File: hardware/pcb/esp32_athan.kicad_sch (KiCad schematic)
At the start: 35 parts, among them J1 USB_C_Receptacle_PowerOnly_6P, J2 02x03_gain, J3 Speaker, J4 OLED, J5 Relay, J6 PROG, SW1 Next, SW2 Select, U1 ESP32-S3-WROOM-1-N16R8, U3 AMS1117-3.3, U4 MAX98357A

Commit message: layout finished and ready for test production
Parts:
- removed J2: 02x03_gain, Package_SO:SOIC-8_3.9x4.9mm_P1.27mm, symbol Connector_Generic:Conn_02x03_Odd_Even
- removed R6: 100k, Package_DIP:DIP-8_W7.62mm, symbol Device:R
- added JP2: SolderJumper_2_Bridged, Jumper:SolderJumper-2_P1.3mm_Bridged_RoundedPad1.0x1.5mm, symbol Jumper:SolderJumper_2_Bridged
- added JP3: SolderJumper_3_Open, Jumper:SolderJumper-3_P1.3mm_Open_RoundedPad1.0x1.5mm, symbol Jumper:SolderJumper_3_Open
- C1: footprint (none) -> Capacitor_THT:CP_Radial_D10.0mm_P5.00mm_P7.50mm
- C2, C6: value 10µF -> 22µF; footprint Package_SO:SOIC-8_3.9x4.9mm_P1.27mm -> Capacitor_SMD:C_1206_3216Metric
- C3, C4, C5, C7: footprint Package_SO:SOIC-8_3.9x4.9mm_P1.27mm -> Capacitor_SMD:C_1206_3216Metric
- D1: footprint (none) -> LED_SMD:LED_1206_3216Metric_Pad1.42x1.75mm_HandSolder
- H1, H2, H3, H4: footprint (none) -> MountingHole:MountingHole_3.2mm_M3
- J3, J5: footprint (none) -> TerminalBlock:TerminalBlock_MaiXu_MX126-5.0-02P_1x02_P5.00mm
- J4: footprint (none) -> Connector_PinHeader_2.54mm:PinHeader_1x04_P2.54mm_Vertical
- J6: footprint (none) -> Connector_PinHeader_2.54mm:PinHeader_1x06_P2.54mm_Vertical
- JP1: footprint (none) -> Jumper:SolderJumper-2_P1.3mm_Bridged_RoundedPad1.0x1.5mm
- R1, R2: value 5.1k -> 4.7k; footprint Package_DIP:DIP-8_W7.62mm -> Resistor_SMD:R_1206_3216Metric
- R10, R5, R8, R9: footprint Package_DIP:DIP-8_W7.62mm -> Resistor_SMD:R_1206_3216Metric
- R11: value 100 -> (100); footprint Package_DIP:DIP-8_W7.62mm -> Resistor_SMD:R_1206_3216Metric
- R3, R4: value 10k -> 4.7k; footprint Package_DIP:DIP-8_W7.62mm -> Resistor_SMD:R_1206_3216Metric
- R7: value 100k -> (100k); footprint Package_DIP:DIP-8_W7.62mm -> Resistor_SMD:R_1206_3216Metric
- SW1, SW2: footprint (none) -> Button_Switch_THT:SW_SPST_Omron_B3F-40xx
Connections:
- net +5V: now also JP3.3 (B)
- net GAIN: now also JP3.2 (C)
- net GND: now also J5.1 (Pin_1), JP2.1 (A); no longer J5.2 (Pin_2)
- net RLY+: now also J5.2 (Pin_2); no longer J5.1 (Pin_1)
- net at R7.1: now also JP2.2 (B), JP3.1 (A)
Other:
- moved on the sheet: J3, J5, R7

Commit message: update schematic and layout with new resistance and new 5-way button instead of select,next
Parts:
- removed SW1: Next, Button_Switch_THT:SW_SPST_Omron_B3F-40xx, symbol Switch:SW_Push
- removed SW2: Select, Button_Switch_THT:SW_SPST_Omron_B3F-40xx, symbol Switch:SW_Push
- added SW1: SKRHABE010, SKRHABE010:SW-SMD_SKRHABE010, symbol SKRHABE010:SKRHABE010
- R5: value 560k -> 4.7k
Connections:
- net BTN_SELECT: now also SW1.2 (CEN)
- net GND: now also SW1.5 (COM)
- net BTN_UP: now reaches U1.22 (IO14)
- net BTN_UP: now also SW1.1 (A)
- net BTN_LEFT: now reaches U1.23 (IO21)
- net BTN_LEFT: now also SW1.3 (C)
- net BTN_RIGHT: now reaches U1.24 (IO47)
- net BTN_RIGHT: now also SW1.4 (D)
- net BTN_NEXT renamed BTN_DOWN
- net BTN_DOWN: now also SW1.6 (B)
- no-connect marks 23 -> 22

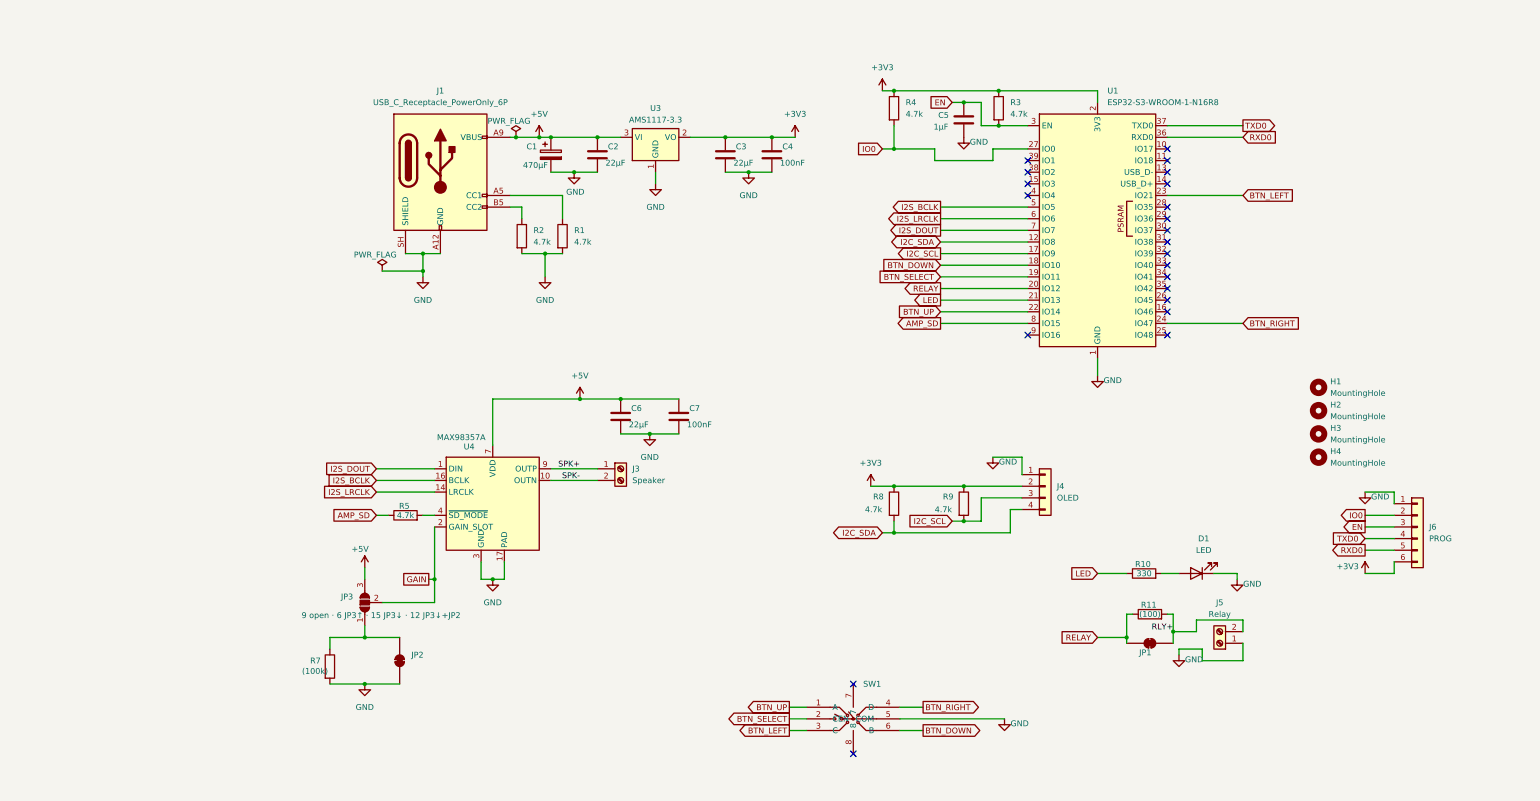
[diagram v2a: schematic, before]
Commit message: Add colour TFT build option, screen settings and the drawn PCB
Display
- The display is chosen at build time: display_type oled|tft, or --display in
  build_firmware.sh and flash_firmware.sh. Each display's code lives in
  firmware/displays/{oled,tft}.yaml. A TFT build has its own release files and
  manifest (manifest-tft.json), so a clock only updates to its own build.
- 240x240 ST7789 TFT (mipi_spi):
  - a ring clock with seconds, flashing 500/500 ms in the last minute
    before an athan;
  - a prayer strip, and mute icons for prayers whose athan is off;
  - a two-pane colour menu with Material Symbols icons;
  - Screen Colour (5 palettes) and a colour Wi-Fi setup screen.
- The OLED drawing is unchanged, behind ATHAN_DISPLAY_TFT. Both displays read
  the menu from one Frame (menu_frame.h).

Screen settings (both displays, menu and web page)
- Brightness 0-100 % (0 % = dark until a key).
- Screen at Night: Off / Dim / Dark, with Night From and Night Until.
- While the screen is dark, a key lights it, dim, for 2 min with a countdown.
- The tick and night windows can end at a prayer (From Maghrib/Isha, Until
  Fajr/Dhuhr), worked out from each day's times (day_window.h, host-tested).
  The window rows are now choices confirmed with Select, with a caption
  previewing the result.

Audio
- Fix a flash preview that kept playing after leaving its menu row: a preview
  still waiting to start is now dropped (cancel_pending_slot_preview_).
- The menu tones are mono 16-bit WAV (no decoding, no MP3 padding). Stored
  sounds stay MP3.

Hardware
- PCB drawn in KiCad: OLED header J4, TFT header J7, 5-way switch footprints
  and 3D models, renders and a STEP export.

README
- 1.1: the clock joins 2.4 GHz Wi-Fi only.
- 1.2 Screen: the OLED's timetable screen and its marks, the colour screen
  (ring, strip, last-minute flash, athan colour, Screen Colour), and the
  dark screen waking on a key.
- 1.3 Menu: two panes, short names, the new rows (Tick From/Until,
  Brightness, Screen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
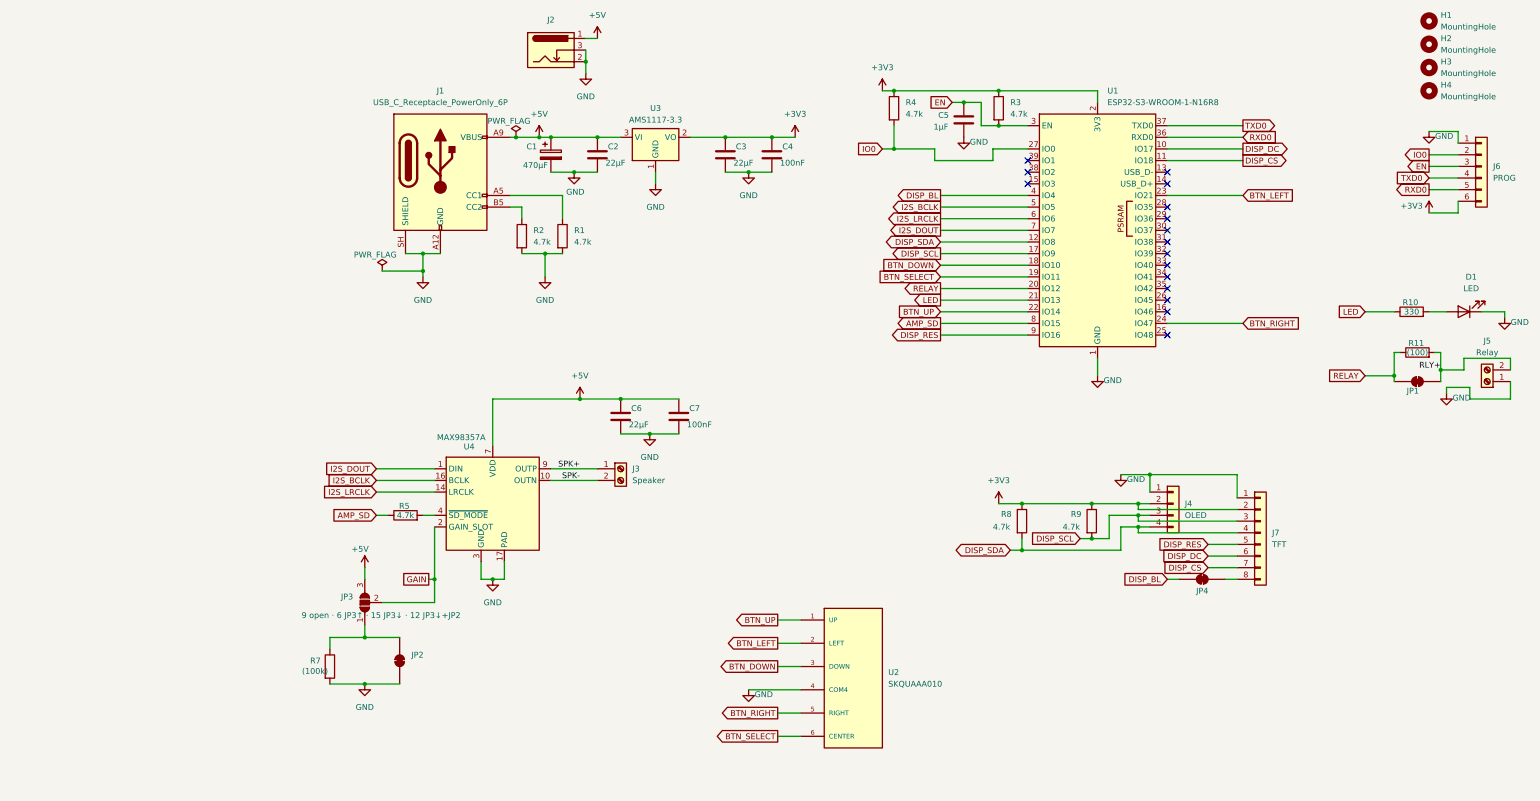
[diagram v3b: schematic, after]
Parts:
- removed SW1: SKRHABE010, SKRHABE010:SW-SMD_SKRHABE010, symbol SKRHABE010:SKRHABE010
- added J2: Barrel_Jack, Connector_BarrelJack:BarrelJack_CUI_PJ-102AH_Horizontal, symbol Connector:Barrel_Jack_Switch
- added J7: TFT, Connector_PinHeader_2.54mm:PinHeader_1x08_P2.54mm_Vertical, symbol Connector_Generic:Conn_01x08
- added JP4: SolderJumper_2_Bridged, Jumper:SolderJumper-2_P1.3mm_Bridged_RoundedPad1.0x1.5mm, symbol Jumper:SolderJumper_2_Bridged
- added U2: SKQUAAA010, SKQUAAA010:SKQUAAA010, symbol SKQUAAA010:SKQUAAA010
- C1: footprint Capacitor_THT:CP_Radial_D10.0mm_P5.00mm_P7.50mm -> Capacitor_SMD:CP_Elec_8x10.5
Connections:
- net +3V3: now also J7.2 (Pin_2)
- net +5V: now also J2.1
- net BTN_DOWN: now also U2.3 (DOWN)
- net BTN_LEFT: now also U2.2 (LEFT)
- net BTN_RIGHT: now also U2.5 (RIGHT)
- net BTN_SELECT: now also U2.6 (CENTER)
- net BTN_UP: now also U2.1 (UP)
- net GND: now also J2.2, J2.3, J7.1 (Pin_1), U2.4 (COM4)
- net DISP_DC: now reaches U1.10 (IO17)
- net DISP_DC: now also J7.6 (Pin_6)
- net DISP_CS: now reaches U1.11 (IO18)
- net DISP_CS: now also J7.7 (Pin_7)
- net DISP_BL: now reaches U1.4 (IO4)
- net DISP_BL: now also JP4.1 (A)
- net DISP_RES: now reaches U1.9 (IO16)
- net DISP_RES: now also J7.5 (Pin_5)
- net I2C_SCL renamed DISP_SCL
- net DISP_SCL: now also J7.3 (Pin_3)
- net I2C_SDA renamed DISP_SDA
- net DISP_SDA: now also J7.4 (Pin_4)
- new net: J7.8 (Pin_8), JP4.2 (B)
- no-connect marks 22 -> 16
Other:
- moved on the sheet: D1, H1, H2, H3, H4, J4, J5, J6, JP1, R10, R11, R8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

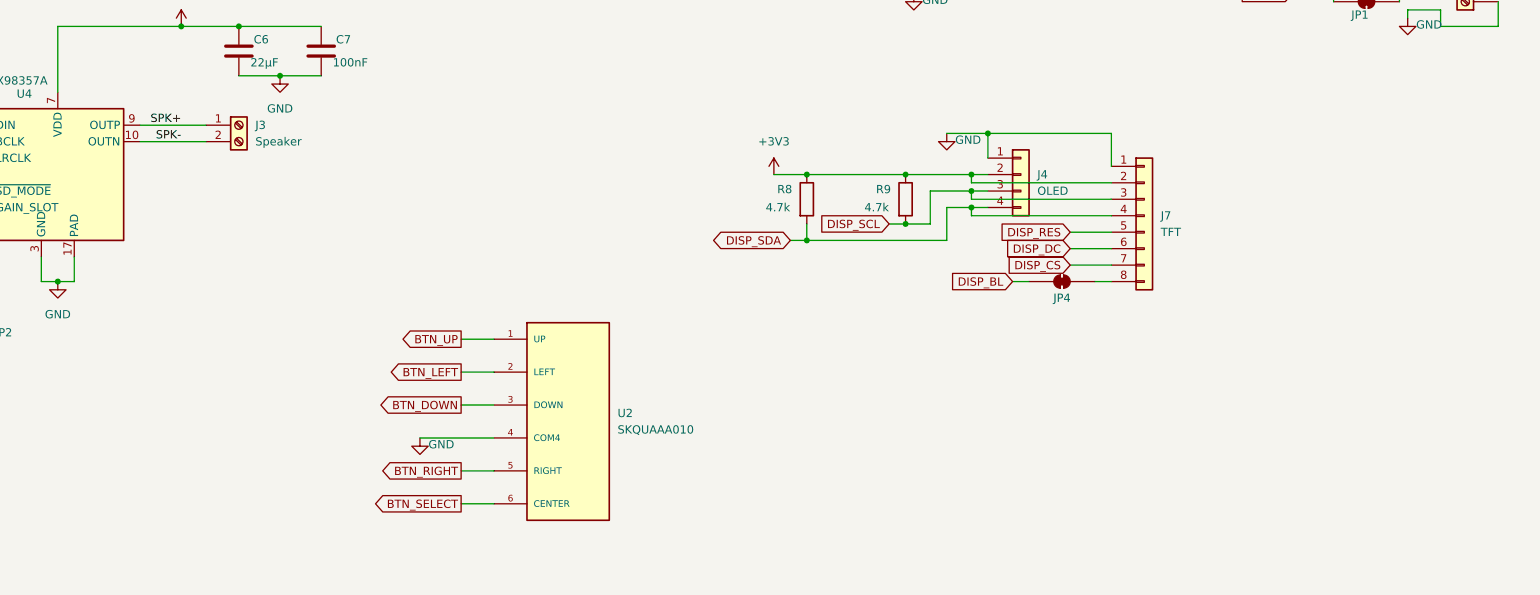
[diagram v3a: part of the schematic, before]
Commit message: Lists of any length, full code review fixes, 44.1 kHz sounds, PCB v5
Sound lists
- The suggested lists (athan, Fajr, tawashih, tick) can have any number of
  entries, numbered in file order ("2. Abdul Basit") in the menu, on /audio
  and on the web page; long names wrap or shorten to fit both displays.
- /audio: one form per sound, with its whole list in a dropdown (the one in
  use marked with a check mark) and Preview / Download buttons; the status
  bar says "downloaded and in use" and offers Reload page when the lists change.
- Radio stays at 10 stations; README shows how to add one from mp3quran.net,
  with screenshots.

Screen and windows
- Tick window: from Fajr or Dhuhr until Maghrib or Isha; night window the
  other way round. An end a window no longer offers becomes an hour at boot.
- Screen at Night: Normal (same as by day) / Dim / Turned off. Normal ignores
  the night window; Dim is never brighter than by day.
- New Night Window line on the web page; both window lines update within
  100 ms of a change.

TFT clock face
- Most seconds redraw only the seconds (about 2.5 ms instead of a 50 ms whole
  face). The whole face is redrawn every 30 s, at each minute, on any change,
  and every second in the last minute.
- The ring is drawn in one pass (tft::ring), pixel-identical to a plain scan
  over 5,820 host-tested cases.
- Frames follow the clock's own second. The last-minute flash is exactly
  500 ms lit / 500 ms dark (measured on the prototype).

Fixes from a full code review (tested on the prototype)
- An upload that broke off left every download "Busy" until a restart.
  It is now freed after 20 s.
- Saving a sound froze the clock for seconds and restarted the I2S speaker
  under the radio. Erases now go block by block with pauses, the radio
  pauses for the write, and the read-back check runs on the worker.
- A stored sound whose end the player lost could not be stopped by the
  5 s bound. Its resampler is now stopped. Joined or damaged MP3 uploads
  a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
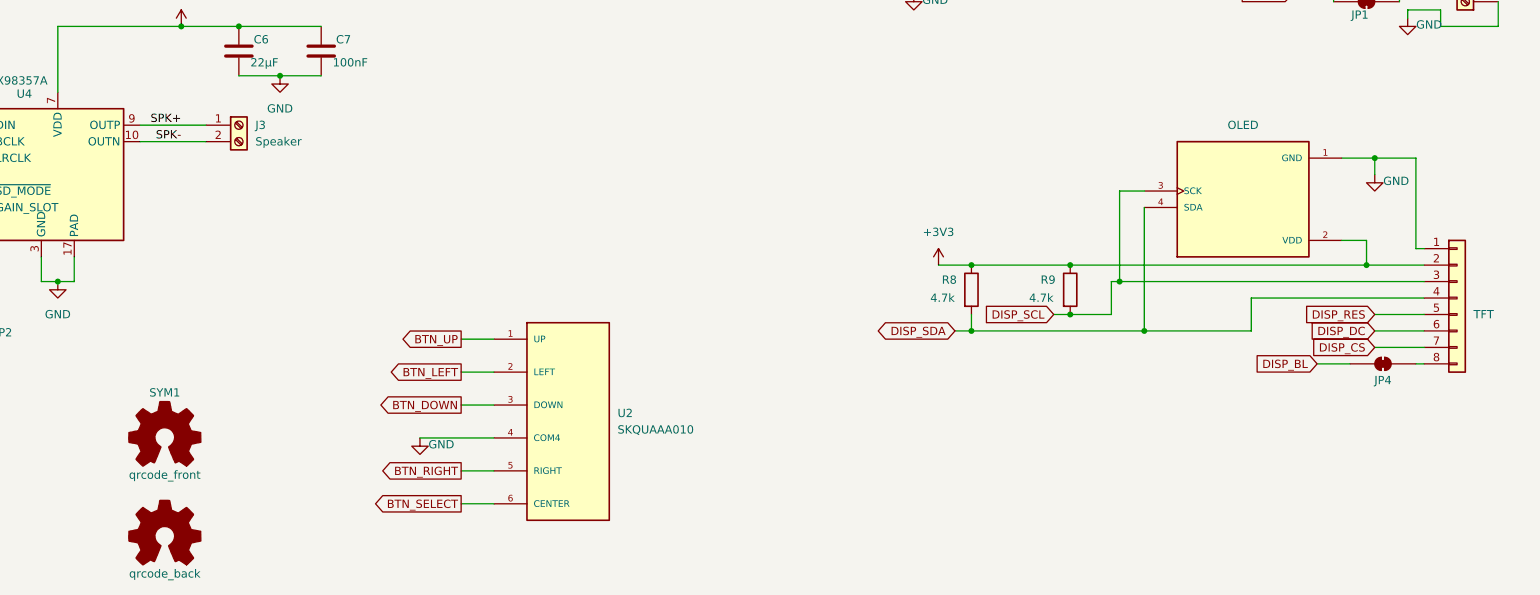
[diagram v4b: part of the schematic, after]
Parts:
- removed J4: OLED, Connector_PinHeader_2.54mm:PinHeader_1x04_P2.54mm_Vertical, symbol Connector_Generic:Conn_01x04
- added DS1: OLED, Library:LCD_OLED_128X64_1.3_I2C, symbol LCD_OLED_128X64_1p3_I2C:OLED_128X64_1.3_I2C
- added SYM1: qrcode_front, Library:QRCode_esp32_athan_p3, symbol Graphic:Logo_Open_Hardware_Small
- added SYM2: qrcode_back, Library:QRCode_esp32_athan_p3, symbol Graphic:Logo_Open_Hardware_Small
- DS2: renamed from J7; footprint Connector_PinHeader_2.54mm:PinHeader_1x08_P2.54mm_Vertical -> Library:Display_TFT_1.54in_ST7789_240x240_8pin
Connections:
- net +3V3: now also DS1.2 (VDD)
- net DISP_SCL: now also DS1.3 (SCK)
- net DISP_SDA: now also DS1.4 (SDA)
- net GND: now also DS1.1 (GND)
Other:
- moved on the sheet: JP4, R8, R9

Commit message: Guides for owners and builders, update mark, JLCPCB assembly files
Docs
- README is now a short landing page: the board picture (front and back,
  to scale, with the 1.54" screen showing the clock), the note for
  version 2 owners, why the prayer times come from this repository, then
  the 2.4 GHz warning, first setup, the joystick, the web page, updates
  and links to the guides.
- New guides/: using.md (setup, screen, keys and menu, web page, sounds,
  radio, prayer times, updates), building.md (prototype, firmware build
  and flash, the board, acceptance checklist), maintaining.md (prayer
  times, sounds, stations, releases) and jlcpcb_assembly.md (ordering the
  board assembled).
- HARDWARE.md rewritten from the KiCad netlist and part positions: power,
  pin map, amplifier, switch, parts list with LCSC numbers and prices,
  layout, enclosure. max98357a_amplifier.md uses the board's part numbers
  and its gain solder jumpers.
- References in the docs, scripts and comments point at the new guides
  and HARDWARE.md sections.
- The Home Assistant key is in using.md section 4. check_docs.py fails if
  it differs from athan.yaml's, and reads the mosque table from using.md.

Firmware updates
- Checked once after each start (30 s after Wi-Fi first connects) and
  daily at 03:00, instead of every 6 h. ESPHome's own start-up check gave
  up when Wi-Fi took more than a minute.
- Never installed by itself (firmware_rules.md 3.2). An update found shows
  as a small up arrow among the status marks on both screens while
  online, and the menu's Update row offers Install. README and using.md
  section 8 show the mark.
- The Update row reads the update's own state: an update found by any
  check shows as Install, and a failed install offers it again ("Install
  failed: try again") instead of staying on "Installing...".
- Firmware Version says "installing 3.0.1 failed, try again" after a
  failed install, not "no release found on GitHub, or no internet".
- Checked: esphome config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
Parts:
- C1: LCSC (none) -> C178530
- C2, C3, C6: LCSC (none) -> C12891
- C4, C7: LCSC (none) -> C24497
- C5: LCSC (none) -> C1848
- D1: LCSC (none) -> C130717
- J1: LCSC (none) -> C3151650
- J2: LCSC (none) -> C3096093
- J3, J5: LCSC (none) -> C5188434
- R1, R2, R3, R4, R5, R8, R9: LCSC (none) -> C17936
- R10: value 330 -> 100; LCSC (none) -> C17901
- R11: LCSC (none) -> C17901; now not fitted
- R7: LCSC (none) -> C17900; now not fitted
- U1: LCSC (none) -> C2913202
- U3: LCSC (none) -> C6186
- U4: LCSC (none) -> C910544
